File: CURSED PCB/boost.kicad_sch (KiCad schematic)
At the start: 6 parts, among them U11 TPS61046YFF

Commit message: something related to current and stuff
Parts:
- renumbered R13 to R12, R14 to R13
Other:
- note added: "24V"
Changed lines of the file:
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@@
 	(generator_version "9.0")
 	(paper "A4")
+	(text "24V"
+		(exclude_from_sim no)
+		(at 152.908 100.584 0)
+		(effects
+			(font
+				(size 1.27 1.27)
+			)
+		)
+	)
 	(junction
 		(at 81.28 101.6)
@@
 		(dnp no)
 		(fields_autoplaced yes)
-		(property "Reference" "R13"
+		(property "Reference" "R12"
 			(at 123.19 121.9199 0)
 			(effects
@@
 			(project "sensor_1"
 				(path "/9fb1a86f-679c-4b88-9ed1-932f4f414580/a884d289-6403-4974-bfe5-5c532984589b"
-					(reference "R13")
+					(reference "R12")
 					(unit 1)
 				)
@@
 		(dnp no)
 		(fields_autoplaced yes)
-		(property "Reference" "R14"
+		(property "Reference" "R13"
 			(at 123.19 109.2199 0)
 			(effects
@@
 			(project "sensor_1"
 				(path "/9fb1a86f-679c-4b88-9ed1-932f4f414580/a884d289-6403-4974-bfe5-5c532984589b"
-					(reference "R14")
+					(reference "R13")
 					(unit 1)
 				)

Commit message: forgot to rename things
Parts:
- L1: footprint (none) -> Inductor_SMD:L_Neosid_SM-NE127_HandSoldering
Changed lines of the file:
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@@
 			)
 		)
-		(property "Footprint" ""
+		(property "Footprint" "Inductor_SMD:L_Neosid_SM-NE127_HandSoldering"
 			(at 95.25 88.9 0)
 			(effects

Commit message: Small changes
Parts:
- L1: footprint Inductor_SMD:L_Neosid_SM-NE127_HandSoldering -> MLF1608E120JTD25:IND_1608_TDK
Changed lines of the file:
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@@
 			)
 		)
-		(property "Footprint" "Inductor_SMD:L_Neosid_SM-NE127_HandSoldering"
+		(property "Footprint" "MLF1608E120JTD25:IND_1608_TDK"
 			(at 95.25 88.9 0)
 			(effects
@@
 			)
 		)
-		(property "Datasheet" "~"
+		(property "Datasheet" "https://www.digikey.ca/en/products/detail/tdk-corporation/MLF1608E120JTD25/4743066"
 			(at 95.25 88.9 0)
 			(effects

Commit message: file
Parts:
- C19, C20: footprint Capacitor_SMD:C_0201_0603Metric_Pad0.64x0.40mm_HandSolder -> Capacitor_SMD:C_0603_1608Metric_Pad1.08x0.95mm_HandSolder
- R12, R13: footprint Resistor_SMD:R_0201_0603Metric -> Resistor_SMD:R_0603_1608Metric_Pad0.98x0.95mm_HandSolder
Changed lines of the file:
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@@
 			)
 		)
-		(property "Footprint" "Capacitor_SMD:C_0201_0603Metric_Pad0.64x0.40mm_HandSolder"
+		(property "Footprint" "Capacitor_SMD:C_0603_1608Metric_Pad1.08x0.95mm_HandSolder"
 			(at 64.4652 111.76 0)
 			(effects
@@
 			)
 		)
-		(property "Footprint" "Resistor_SMD:R_0201_0603Metric"
+		(property "Footprint" "Resistor_SMD:R_0603_1608Metric_Pad0.98x0.95mm_HandSolder"
 			(at 119.634 122.936 90)
 			(effects
@@
 			)
 		)
-		(property "Footprint" "Capacitor_SMD:C_0201_0603Metric_Pad0.64x0.40mm_HandSolder"
+		(property "Footprint" "Capacitor_SMD:C_0603_1608Metric_Pad1.08x0.95mm_HandSolder"
 			(at 135.5852 119.38 0)
 			(effects
@@
 			)
 		)
-		(property "Footprint" "Resistor_SMD:R_0201_0603Metric"
+		(property "Footprint" "Resistor_SMD:R_0603_1608Metric_Pad0.98x0.95mm_HandSolder"
 			(at 119.634 110.236 90)
 			(effects

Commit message: redone pcb
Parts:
- C19, C20: footprint Capacitor_SMD:C_0603_1608Metric_Pad1.08x0.95mm_HandSolder -> Capacitor_SMD:C_0805_2012Metric_Pad1.18x1.45mm_HandSolder
- R12, R13: footprint Resistor_SMD:R_0603_1608Metric_Pad0.98x0.95mm_HandSolder -> Resistor_SMD:R_0805_2012Metric_Pad1.20x1.40mm_HandSolder
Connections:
- net GND renamed AGND
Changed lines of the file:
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@@
 			)
 		)
-		(property "Footprint" "Capacitor_SMD:C_0603_1608Metric_Pad1.08x0.95mm_HandSolder"
+		(property "Footprint" "Capacitor_SMD:C_0805_2012Metric_Pad1.18x1.45mm_HandSolder"
 			(at 64.4652 111.76 0)
 			(effects
@@
 			)
 		)
-		(property "Value" "GND"
+		(property "Value" "AGND"
 			(at 95.25 133.35 0)
 			(effects
@@
 			)
 		)
-		(property "Footprint" "Resistor_SMD:R_0603_1608Metric_Pad0.98x0.95mm_HandSolder"
+		(property "Footprint" "Resistor_SMD:R_0805_2012Metric_Pad1.20x1.40mm_HandSolder"
 			(at 119.634 122.936 90)
 			(effects
@@
 			)
 		)
-		(property "Footprint" "Capacitor_SMD:C_0603_1608Metric_Pad1.08x0.95mm_HandSolder"
+		(property "Footprint" "Capacitor_SMD:C_0805_2012Metric_Pad1.18x1.45mm_HandSolder"
 			(at 135.5852 119.38 0)
 			(effects
@@
 			)
 		)
-		(property "Value" "GND"
-			(at 63.5 118.11 0)
-			(effects
-				(font
-					(size 1.27 1.27)
-				)
+		(property "Value" "AGND"
+			(at 66.04 114.2999 0)
+			(effects
+				(font
+					(size 1.27 1.27)
+				)
+				(justify left)
 			)
 		)
@@
 			)
 		)
-		(property "Footprint" "Resistor_SMD:R_0603_1608Metric_Pad0.98x0.95mm_HandSolder"
+		(property "Footprint" "Resistor_SMD:R_0805_2012Metric_Pad1.20x1.40mm_HandSolder"
 			(at 119.634 110.236 90)
 			(effects

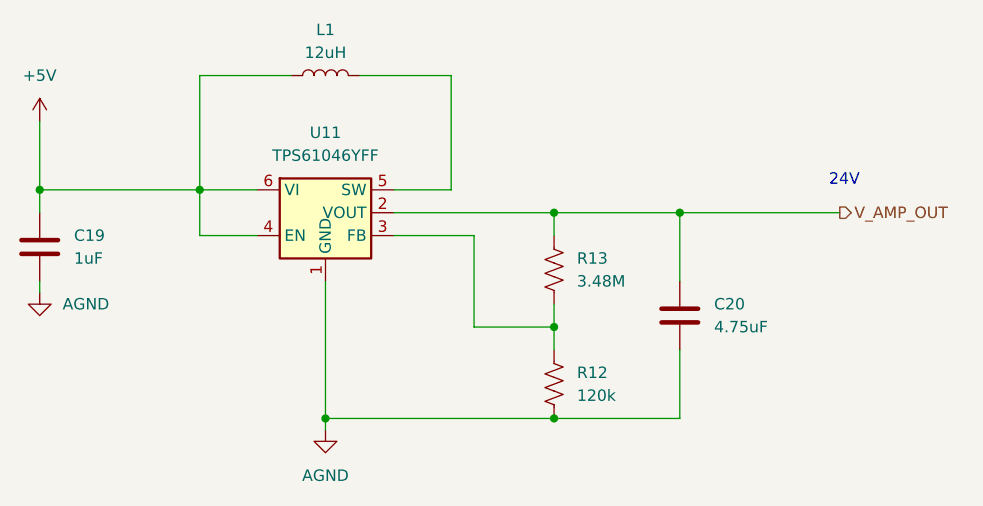
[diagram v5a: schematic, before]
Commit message: no spilt-ground plane (bad idea)
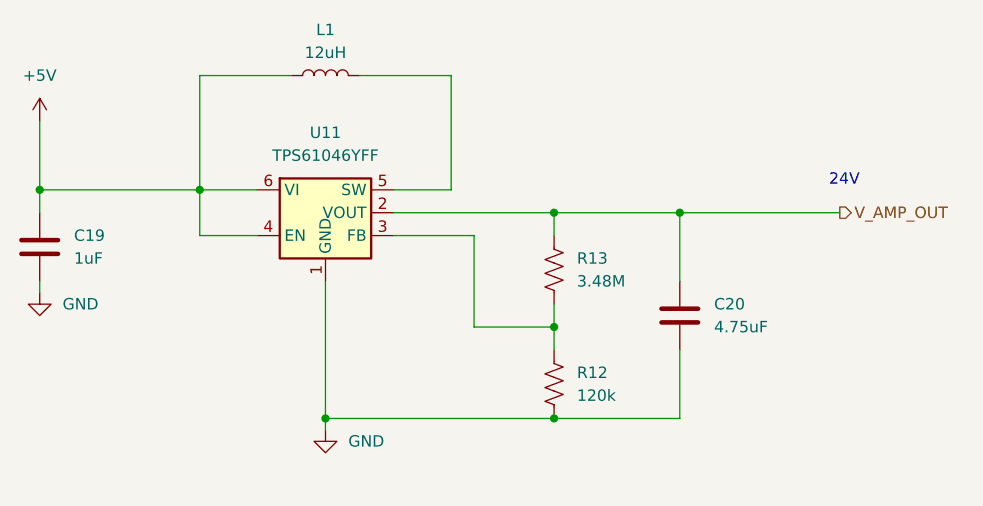
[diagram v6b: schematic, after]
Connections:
- net AGND renamed GND
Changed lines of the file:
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@@
 			)
 		)
-		(property "Value" "AGND"
-			(at 95.25 133.35 0)
-			(effects
-				(font
-					(size 1.27 1.27)
-				)
+		(property "Value" "GND"
+			(at 97.79 129.5399 0)
+			(effects
+				(font
+					(size 1.27 1.27)
+				)
+				(justify left)
 			)
 		)
@@
 			)
 		)
-		(property "Value" "AGND"
+		(property "Value" "GND"
 			(at 66.04 114.2999 0)
 			(effects

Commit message: fixes from darian review
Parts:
- U11: value TPS61046YFF -> TPS61046YFFR; Name (none) -> TPS61046YFFR
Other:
- note added: "Name: TPS61046YFFR idk why its not updating"
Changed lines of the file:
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@@
+		)
+	)
+	(text "Name: TPS61046YFFR\nidk why its not updating"
+		(exclude_from_sim no)
+		(at 120.396 95.25 0)
+		(effects
+			(font
+				(size 1.27 1.27)
+			)
 		)
 	)
@@
 			)
 		)
-		(property "Value" "TPS61046YFF"
+		(property "Value" "TPS61046YFFR"
 			(at 95.25 97.79 0)
 			(effects
@@
 			(at 95.25 106.68 0)
 			(effects
+				(font
+					(size 1.27 1.27)
+				)
+				(hide yes)
+			)
+		)
+		(property "Name" "TPS61046YFFR"
+			(at 95.25 106.68 0)
+			(effects

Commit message: Fixes to pranav sugestions
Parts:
- R13: value 3.48M -> 2.76M
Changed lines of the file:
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@@
 			)
 		)
-		(property "Value" "3.48M"
+		(property "Value" "2.76M"
 			(at 123.19 111.7599 0)
 			(effects
